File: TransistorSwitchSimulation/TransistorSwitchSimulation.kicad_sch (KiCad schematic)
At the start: 5 parts, among them Q1 PN2222A

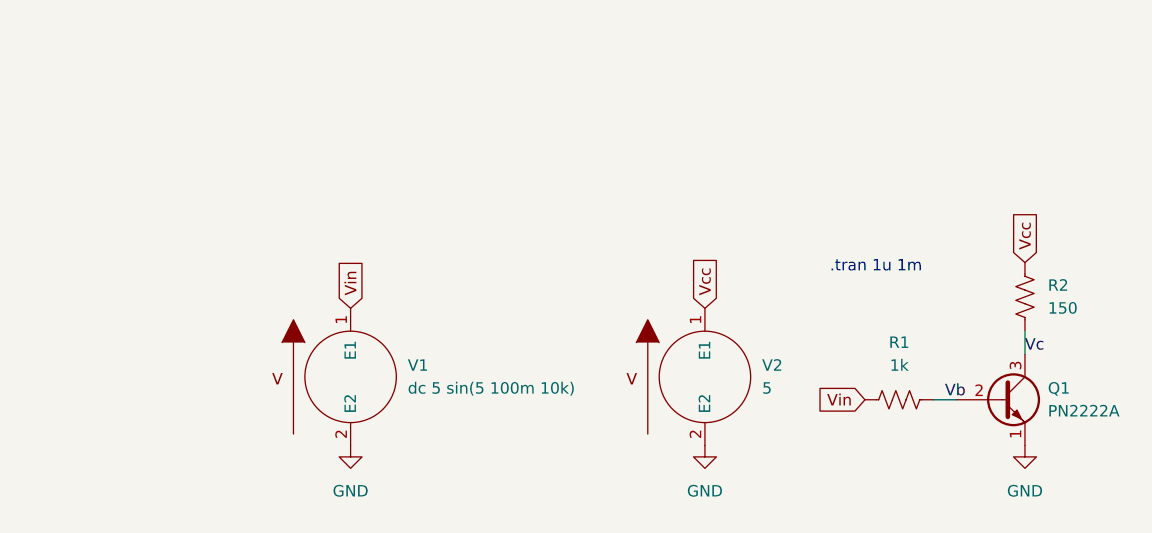
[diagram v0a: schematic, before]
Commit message: Converted project for KiCad 7 compatibility and added Ve net label.
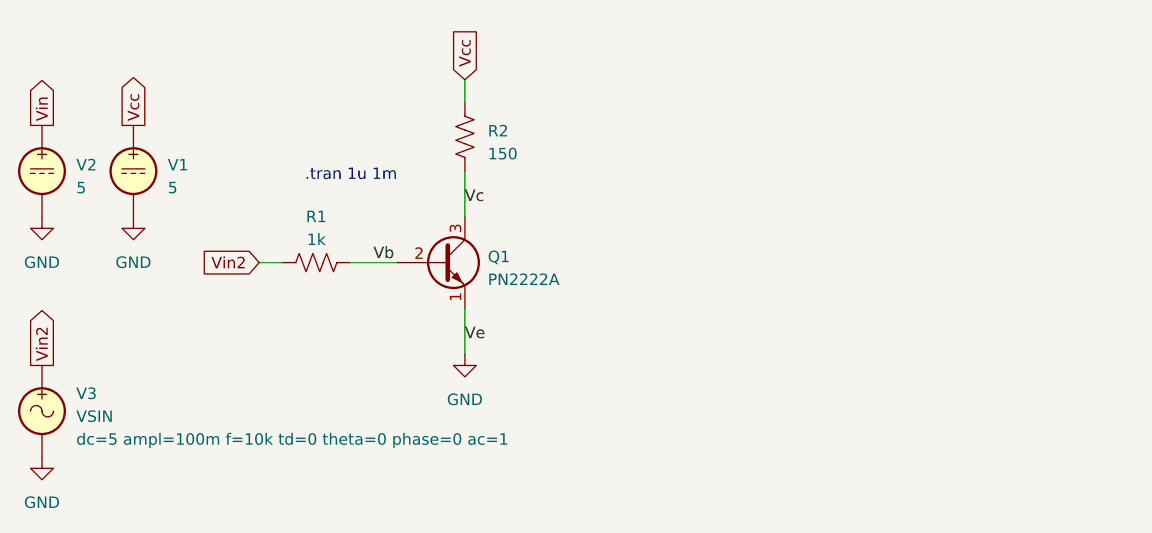
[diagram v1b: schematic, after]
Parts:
- removed V1: dc 5 sin(5 100m 10k), symbol pspice:VSOURCE
- removed V2: 5, symbol pspice:VSOURCE
- added V1, V2: 5, symbol Simulation_SPICE:VDC
- added V3: VSIN, symbol Simulation_SPICE:VSIN
- Q1: Spice_Lib_File PN2222A.lib -> (none); Spice_Model PN2222A -> (none); Spice_Netlist_Enabled Y -> (none); Spice_Node_Sequence 3 2 1 -> (none); Spice_Primitive Q -> (none)
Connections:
- net GND: now also V1.2, V2.2, V3.2
- net Vcc: now also V1.1
- net Vin: now also V2.1; no longer R1.1
- new net Vin2: R1.1, V3.1
